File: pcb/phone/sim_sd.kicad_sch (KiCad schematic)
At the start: 7 parts, among them U10 ESDA6V1-5SC6, U11 ESDA6V1-5SC6

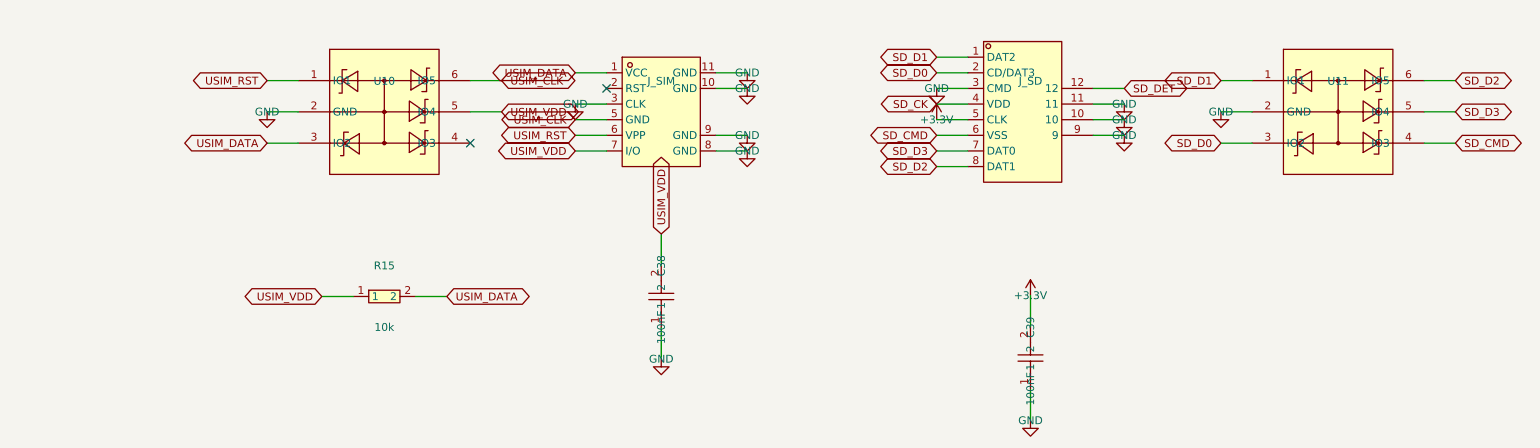
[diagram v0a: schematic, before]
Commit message: User edits: keypad rewiring, sheet reorder, ERC severity reverts, R24 fix
Keypad (keypad.kicad_sch):
- Rotated all 20 switches 270 degrees for vertical contact orientation
- Wired all 4 pins on each switch (pins 1&2 to column, pins 3&4 to row)
- Removed all 37 no_connect markers on pins 3&4
- Cleaned up to 25.4mm (1-inch) grid spacing
- Added pull-down resistors to all 4 columns (was only KEY_COL3)

Root sheet (phone.kicad_sch):
- Reordered sub-sheet blocks (Display_Daughter before SIM_SD)
- Cleaned up PWR_FLAG symbol formatting/indentation
- Reordered PWR_FLAG and +BATT symbol placement

MCU sheet (mcu.kicad_sch):
- Repositioned +3.3V power symbol (#PWR32) at pin 190.5,200.66

Project settings (phone.kicad_pro):
- Reverted ERC suppressions: endpoint_off_grid, isolated_pin_label,
  lib_symbol_mismatch back to warning (want actual fixes, not ignores)
- Added SW2-20 to used designators
- Reordered sheets list (Display_Daughter before SIM_SD)

Other sheets (codec, display, display_daughter, sim_sd):
- KiCad editor reformatting upon save

Generated with [Devin](https://devin.ai)

Co-Authored-By: Devin <158243242+devin-ai-integration[bot]@users.noreply.github.com>
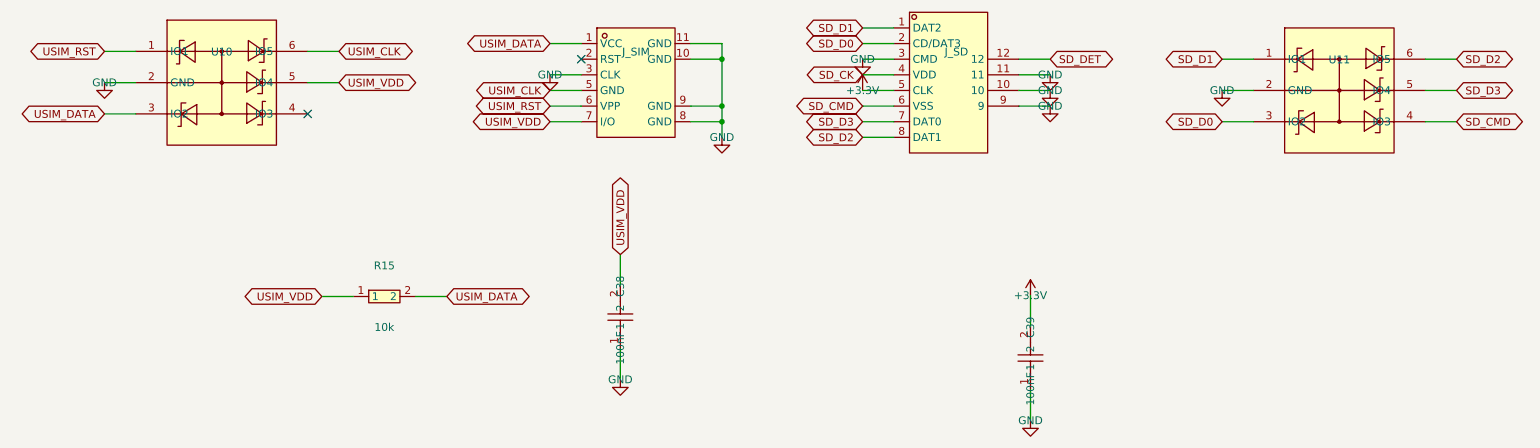
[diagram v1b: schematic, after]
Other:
- moved on the sheet: C38, J_SD, J_SIM, U10, U11
